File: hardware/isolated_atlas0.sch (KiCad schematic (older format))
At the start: 15 parts, among them J201 CONN_01X02, P2 ATLAS_EC_PROBE, U201 ADM3260, U202 ATLAS_EC

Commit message: Upgrade to Kicad 5.
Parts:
- C201, C202, C203, C204, C205, C206: symbol C -> fk-atlas-rescue:C
- J201: symbol CONN_01X02 -> fk-atlas-rescue:CONN_01X02
- P2: symbol WATER_PROBE -> fk-atlas-rescue:WATER_PROBE
- R201, R202, R203, R204, R205: symbol R -> fk-atlas-rescue:R
- U201: symbol adm3260 -> fk-atlas-rescue:adm3260
- U202: symbol ATLAS_SENSOR -> conservify:ATLAS_SENSOR
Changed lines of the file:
@@
-EESchema Schematic File Version 2
-LIBS:conservify
+EESchema Schematic File Version 4
 LIBS:fk-atlas-cache
-EELAYER 25 0
+EELAYER 26 0
 EELAYER END
 $Descr A4 11693 8268
@@
 $EndDescr
 $Comp
-L adm3260 U201
+L fk-atlas-rescue:adm3260 U201
 U 1 1 5948D478
 P 4400 2900
@@
 $EndComp
 $Comp
-L C C203
+L fk-atlas-rescue:C C203
 U 1 1 594C2CF3
 P 5650 3800
@@
 $EndComp
 $Comp
-L C C204
+L fk-atlas-rescue:C C204
 U 1 1 5948D57F
 P 5650 4100
@@
 $EndComp
 $Comp
-L C C205
+L fk-atlas-rescue:C C205
 U 1 1 594C2CFE
 P 5650 4400
@@
 $EndComp
 $Comp
-L C C206
+L fk-atlas-rescue:C C206
 U 1 1 594C2D01
 P 5650 4650
@@
 $EndComp
 $Comp
-L C C201
+L fk-atlas-rescue:C C201
 U 1 1 594C2D06
 P 2900 3800
@@
 $EndComp
 $Comp
-L C C202
+L fk-atlas-rescue:C C202
 U 1 1 594C2D08
 P 2900 4100
@@
 $EndComp
 $Comp
-L R R201
+L fk-atlas-rescue:R R201
 U 1 1 594C2D0E
 P 5650 3300
@@
 $EndComp
 $Comp
-L R R202
+L fk-atlas-rescue:R R202
 U 1 1 594C2D12
 P 6250 2700
@@
 $EndComp
 $Comp
-L R R204
+L fk-atlas-rescue:R R204
 U 1 1 5948E389
 P 6700 2700
@@
 $EndComp
 $Comp
-L R R203
+L fk-atlas-rescue:R R203
 U 1 1 594C2D17
 P 6300 3250
@@
 $EndComp
 $Comp
-L R R205
+L fk-atlas-rescue:R R205
 U 1 1 594C2D1E
 P 6800 3250
@@
 $EndComp
 $Comp
-L VCC #PWR057
+L fk-atlas-rescue:VCC #PWR057
 U 1 1 594C2D26
 P 2450 3750
@@
 $EndComp
 $Comp
-L VCC #PWR058
+L fk-atlas-rescue:VCC #PWR058
 U 1 1 594C2D28
 P 2450 2350
@@
 $EndComp
 $Comp
-L ATLAS_SENSOR U202
+L conservify:ATLAS_SENSOR U202
 U 1 1 594C2D33
 P 8550 2900
@@
 $EndComp
 $Comp
-L CONN_01X02 J201
+L fk-atlas-rescue:CONN_01X02 J201
 U 1 1 59A1BC7B
 P 10050 2950
@@
 $EndComp
 $Comp
-L WATER_PROBE P2
+L fk-atlas-rescue:WATER_PROBE P2
 U 1 1 59D297CD
 P 8800 3550

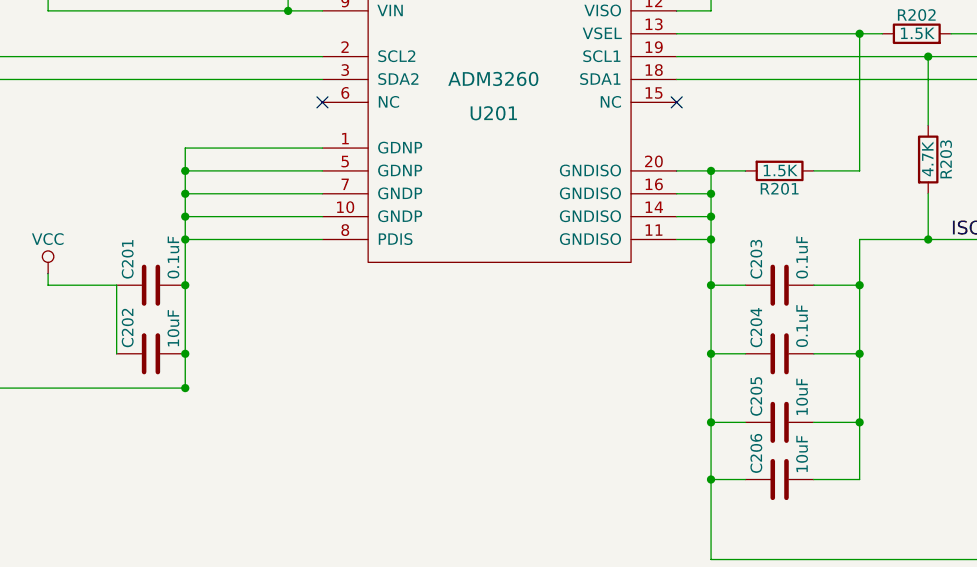
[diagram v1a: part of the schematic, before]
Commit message: Consistent part values across our schematics.
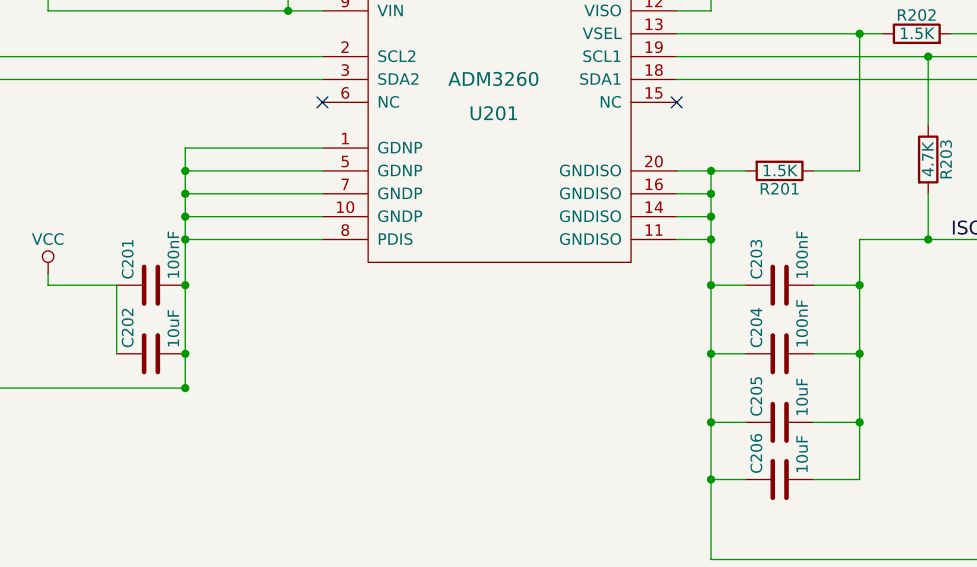
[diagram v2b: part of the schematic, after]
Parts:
- C201, C203, C204: value 0.1uF -> 100nF

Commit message: Part updates.
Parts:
- C201, C203, C204: Critical (none) -> (none); MFN (none) -> Murata Electronics; MFP (none) -> GRM188R71H104KA93D; Notes (none) -> (none); Package (none) -> (none); Source (none) -> ANY; Subsystem (none) -> (none); Supplier1 (none) -> mouser
- C202, C205, C206: Critical (none) -> (none); MFN (none) -> Taiyo Yuden; MFP (none) -> LMK107BBJ106KALT; Notes (none) -> (none); Package (none) -> (none); Source (none) -> ANY; Subsystem (none) -> (none); Supplier1 (none) -> mouser; spn1 81-GRM188R60J106ME47 -> 963-LMK107BBJ106KALT
- J201: Critical (none) -> (none); MFN (none) -> Amphenol RF; MFP (none) -> 031-5431; Notes (none) -> (none); Package (none) -> (none); Source (none) -> ANY; Subsystem (none) -> (none); Supplier1 (none) -> mouser
- P2: Critical (none) -> (none); MFN (none) -> (none); MFP (none) -> (none); Notes (none) -> (none); Package (none) -> (none); SPN1 (none) -> (none); Source (none) -> ANY; Subsystem (none) -> (none); Supplier1 (none) -> (none)
- R201, R202, R204: Critical (none) -> (none); MFN (none) -> (none); MFP (none) -> (none); Notes (none) -> (none); Package (none) -> (none); Source (none) -> ANY; Subsystem (none) -> (none); Supplier1 (none) -> (none)
- R203, R205: Critical (none) -> (none); MFN (none) -> Yageo; MFP (none) -> AF0603JR-074K7L; Notes (none) -> (none); Package (none) -> (none); Source (none) -> ANY; Subsystem (none) -> (none); Supplier1 (none) -> mouser
- U201: Critical (none) -> (none); MFN (none) -> Analog Devices / Linear Technology; MFP (none) -> ADM3260ARSZ; Notes (none) -> (none); Package (none) -> (none); Source (none) -> ANY; Subsystem (none) -> (none); Supplier1 (none) -> mouser
- U202: Critical (none) -> (none); MFN (none) -> (none); MFP (none) -> (none); Notes (none) -> (none); Package (none) -> (none); SPN1 (none) -> (none); Source (none) -> ANY; Subsystem (none) -> (none); Supplier1 (none) -> atlas

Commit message: Fix DRC in schematic mode.
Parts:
- C201, C202, C203, C204, C205, C206: symbol fk-atlas-rescue:C -> conservify:CAPACITOR_CERAMIC
- J201: symbol fk-atlas-rescue:CONN_01X02 -> conservify:CONN_01x02
- P2: symbol fk-atlas-rescue:WATER_PROBE -> conservify:ATLAS_WATER_PROBE
- R201, R202, R203, R204, R205: symbol fk-atlas-rescue:R -> conservify:R
- U201: symbol fk-atlas-rescue:adm3260 -> conservify:ADM3260
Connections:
- wire segments 52 -> 78
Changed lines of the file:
@@
 $EndDescr
 $Comp
-L fk-atlas-rescue:adm3260 U201
+L conservify:ADM3260 U201
 U 1 1 5948D478
 P 4400 2900
@@
 $EndComp
 $Comp
-L fk-atlas-rescue:C C203
+L conservify:CAPACITOR_CERAMIC C203
 U 1 1 594C2CF3
 P 5650 3800
@@
 $EndComp
 $Comp
-L fk-atlas-rescue:C C204
+L conservify:CAPACITOR_CERAMIC C204
 U 1 1 5948D57F
 P 5650 4100
@@
 $EndComp
 $Comp
-L fk-atlas-rescue:C C205
+L conservify:CAPACITOR_CERAMIC C205
 U 1 1 594C2CFE
 P 5650 4400
@@
 $EndComp
 $Comp
-L fk-atlas-rescue:C C206
+L conservify:CAPACITOR_CERAMIC C206
 U 1 1 594C2D01
 P 5650 4650
@@
 $EndComp
 $Comp
-L fk-atlas-rescue:C C201
+L conservify:CAPACITOR_CERAMIC C201
 U 1 1 594C2D06
 P 2900 3800
@@
 $EndComp
 $Comp
-L fk-atlas-rescue:C C202
+L conservify:CAPACITOR_CERAMIC C202
 U 1 1 594C2D08
 P 2900 4100
@@
 $EndComp
 $Comp
-L fk-atlas-rescue:R R201
+L conservify:R R201
 U 1 1 594C2D0E
 P 5650 3300
@@
 $EndComp
 $Comp
-L fk-atlas-rescue:R R202
+L conservify:R R202
 U 1 1 594C2D12
 P 6250 2700
@@
 $EndComp
 $Comp
-L fk-atlas-rescue:R R204
+L conservify:R R204
 U 1 1 5948E389
 P 6700 2700
@@
 $EndComp
 $Comp
-L fk-atlas-rescue:R R203
+L conservify:R R203
 U 1 1 594C2D17
 P 6300 3250
@@
 $EndComp
 $Comp
-L fk-atlas-rescue:R R205
+L conservify:R R205
 U 1 1 594C2D1E
 P 6800 3250
@@
 $EndComp
 $Comp
-L fk-atlas-rescue:VCC #PWR057
+L conservify:VCC #PWR057
 U 1 1 594C2D26
 P 2450 3750
@@
 $EndComp
 $Comp
-L fk-atlas-rescue:VCC #PWR058
+L conservify:VCC #PWR058
 U 1 1 594C2D28
 P 2450 2350
@@
 $EndComp
 $Comp
-L fk-atlas-rescue:CONN_01X02 J201
+L conservify:CONN_01x02 J201
 U 1 1 59A1BC7B
-P 10050 2950
-F 0 "J201" H 10050 3100 50  0000 C CNN
-F 1 "CONN_01X02" V 10150 2950 50  0000 C CNN
-F 2 "conservify:BNC" H 10050 2950 50  0001 C CNN
-F 3 "" H 10050 2950 50  0001 C CNN
-F 4 " " H 10050 3200 50  0001 C CNN "Critical"
-F 5 "Amphenol RF" H 10050 3200 50  0001 C CNN "MFN"
-F 6 "031-5431" H 10050 3200 50  0001 C CNN "MFP"
-F 7 " " H 10050 3200 50  0001 C CNN "Notes"
-F 8 " " H 10050 3200 50  0001 C CNN "Package"
-F 9 "ANY" H 10050 3200 50  0001 C CNN "Source"
-F 10 " " H 10050 3200 50  0001 C CNN "Subsystem"
-F 11 "mouser" H 10050 3200 50  0001 C CNN "Supplier1"
-F 12 "0" H 10050 3200 50  0001 C CNN "price"
-F 13 "523-31-5431" H 200 0   50  0001 C CNN "spn1"
-	1    10050 2950
-	1    0    0    -1
-$EndComp
-$Comp
-L fk-atlas-rescue:WATER_PROBE P2
+P 10050 2900
+F 0 "J201" H 10050 3050 50  0000 C CNN
+F 1 "CONN_01X02" V 10150 2900 50  0000 C CNN
+F 2 "conservify:BNC" H 10050 2900 50  0001 C CNN
+F 3 "" H 10050 2900 50  0001 C CNN
+F 4 " " H 10050 3150 50  0001 C CNN "Critical"
+F 5 "Amphenol RF" H 10050 3150 50  0001 C CNN "MFN"
+F 6 "031-5431" H 10050 3150 50  0001 C CNN "MFP"
+F 7 " " H 10050 3150 50  0001 C CNN "Notes"
+F 8 " " H 10050 3150 50  0001 C CNN "Package"
+F 9 "ANY" H 10050 3150 50  0001 C CNN "Source"
+F 10 " " H 10050 3150 50  0001 C CNN "Subsystem"
+F 11 "mouser" H 10050 3150 50  0001 C CNN "Supplier1"
+F 12 "0" H 10050 3150 50  0001 C CNN "price"
+F 13 "523-31-5431" H 200 -50 50  0001 C CNN "spn1"
+	1    10050 2900
+	1    0    0    -1
+$EndComp
+$Comp
+L conservify:ATLAS_WATER_PROBE P2
 U 1 1 59D297CD
 P 8800 3550
@@
 F 12 " " H 8800 3650 50  0001 C CNN "Supplier1"
 	1    8800 3550
+	1    0    0    -1
+$EndComp
+$Comp
+L conservify:PWR_FLAG #FLG0106
+U 1 1 5BCC03FC
+P 7400 4900
+F 0 "#FLG0106" H 7400 4975 50  0001 C CNN
+F 1 "PWR_FLAG" H 7400 5050 50  0000 C CNN
+F 2 "" H 7400 4900 50  0001 C CNN
+F 3 "~" H 7400 4900 50  0001 C CNN
+	1    7400 4900
 	1    0    0    -1
 $EndComp
@@
 EC_PGND
 Wire Wire Line
-	5200 3300 5500 3300
-Wire Wire Line
-	5350 3300 5350 5000
+	5200 3300 5350 3300
+Wire Wire Line
+	5350 3300 5350 3400
 Wire Wire Line
 	5350 3600 5200 3600
@@
 	5800 3800 6000 3800
 Wire Wire Line
-	6000 3600 6000 4650
+	6000 3600 6000 3800
 Wire Wire Line
 	6000 4650 5800 4650
@@
 	5800 4100 6000 4100
 Wire Wire Line
-	5200 2800 7800 2800
-Wire Wire Line
-	5200 2900 7800 2900
-Wire Wire Line
-	5200 2700 6100 2700
+	5200 2800 6300 2800
+Wire Wire Line
+	5200 2900 6800 2900
+Wire Wire Line
+	5200 2700 6000 2700
 Wire Wire Line
 	6000 2700 6000 3300
@@
 	5350 2600 5350 2500
 Wire Wire Line
-	5200 2500 7400 2500
+	5200 2500 5350 2500
 Wire Wire Line
 	6900 2500 6900 2700
@@
 	6300 3400 6300 3600
 Wire Wire Line
-	6000 3600 6800 3600
+	6000 3600 6300 3600
 Wire Wire Line
 	6800 3600 6800 3400
 Wire Wire Line
-	2450 2600 3650 2600
-Wire Wire Line
-	2450 2350 2450 2600
+	2450 2600 3500 2600
+Wire Wire Line
+	2450 2350 2450 2450
 Wire Wire Line
 	3650 2500 3500 2500
@@
 	3650 3200 3050 3200
 Wire Wire Line
-	3050 3200 3050 4250
+	3050 3200 3050 3300
 Wire Wire Line
 	3050 4250 1750 4250
@@
 Wire Wire Line
 	9450 3000 9850 3000
+Wire Wire Line
+	5350 3500 5350 3600
+Wire Wire Line
+	5350 3400 5350 3500
+Wire Wire Line
+	5350 3600 5350 3800
+Wire Wire Line
+	5350 4400 5350 4650
+Wire Wire Line
+	5350 4100 5350 4400
+Wire Wire Line
+	5350 3800 5350 4100
+Wire Wire Line
+	6000 4400 6000 4650
+Wire Wire Line
+	6000 4100 6000 4400
+Wire Wire Line
+	5350 3300 5500 3300
+Wire Wire Line
+	5350 2500 6900 2500
+Wire Wire Line
+	6000 2700 6100 2700
+Wire Wire Line
+	6300 2800 7800 2800
+Wire Wire Line
+	6800 2900 7800 2900
+Wire Wire Line
+	3500 2600 3650 2600
+Wire Wire Line
+	3050 3800 3050 4100
+Wire Wire Line
+	3050 4100 3050 4250
+Wire Wire Line
+	3050 3600 3050 3800
+Wire Wire Line
+	3050 3500 3050 3600
+Wire Wire Line
+	3050 3400 3050 3500
+Wire Wire Line
+	3050 3300 3050 3400
+Wire Wire Line
+	2450 2450 2450 2600
+Wire Wire Line
+	5350 4650 5350 5000
+Wire Wire Line
+	6300 3600 6800 3600
+Wire Wire Line
+	6000 3800 6000 4100
+Wire Wire Line
+	6900 2500 7400 2500
+Wire Wire Line
+	7400 4900 7400 5000
 Connection ~ 5350 3500
 Connection ~ 5350 3400
@@
 Connection ~ 6300 3600
 Connection ~ 6000 3800
-Connection ~ 3050 4250
 Connection ~ 6900 2500
 NoConn ~ 3650 3000

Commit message: Drop prototype Atlas modules - focus on getting OEM boards working.
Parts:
- U202: footprint conservify:ATLAS_SENSOR_BOARD_COMBO -> conservify:ATLAS_SENSOR_BOARD_OEM
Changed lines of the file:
@@
 F 0 "U202" H 8150 2550 60  0000 C CNN
 F 1 "ATLAS_EC" H 8600 2850 60  0000 C CNN
-F 2 "conservify:ATLAS_SENSOR_BOARD_COMBO" H 8550 2900 60  0001 C CNN
+F 2 "conservify:ATLAS_SENSOR_BOARD_OEM" H 8550 2900 60  0001 C CNN
 F 3 "" H 8550 2900 60  0001 C CNN
 F 4 " " H 8150 2650 50  0001 C CNN "Critical"

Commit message: Trying out some test points.
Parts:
- added J10, J9: CONN_01x02, conservify:TP_Pads_D1.5mm_1x2, symbol conservify:CONN_01x02
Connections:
- wire segments 78 -> 82
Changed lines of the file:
@@
 NoConn ~ 3650 3000
 NoConn ~ 5200 3000
+Text Label 8350 4450 0    60   ~ 0
+ISO_GND
+Text Label 8350 4350 0    60   ~ 0
+ISO_VCC
+Text Label 8350 4100 0    60   ~ 0
+ISO_SCL
+Text Label 8350 4200 0    60   ~ 0
+ISO_SDA
+Wire Wire Line
+	8350 4100 8750 4100
+Wire Wire Line
+	8750 4200 8350 4200
+Wire Wire Line
+	8350 4350 8750 4350
+Wire Wire Line
+	8750 4450 8350 4450
+$Comp
+L conservify:CONN_01x02 J9
+U 1 1 5C0B31F6
+P 8950 4100
+F 0 "J9" H 9029 4092 50  0000 L CNN
+F 1 "CONN_01x02" H 9029 4001 50  0000 L CNN
+F 2 "conservify:TP_Pads_D1.5mm_1x2" H 8950 4100 50  0001 C CNN
+F 3 "" H 8950 4100 50  0001 C CNN
+	1    8950 4100
+	1    0    0    -1
+$EndComp
+$Comp
+L conservify:CONN_01x02 J10
+U 1 1 5C0B3270
+P 8950 4350
+F 0 "J10" H 9029 4342 50  0000 L CNN
+F 1 "CONN_01x02" H 9029 4251 50  0000 L CNN
+F 2 "conservify:TP_Pads_D1.5mm_1x2" H 8950 4350 50  0001 C CNN
+F 3 "" H 8950 4350 50  0001 C CNN
+	1    8950 4350
+	1    0    0    -1
+$EndComp
 $EndSCHEMATC

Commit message: Add orientation indicator to SWD fp.
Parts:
- J10, J9: Critical (none) -> (none); MFN (none) -> (none); MFP (none) -> (none); Notes (none) -> (none); Package (none) -> (none); SPN1 (none) -> (none); Source (none) -> ANY; Subsystem (none) -> (none); Supplier1 (none) -> (none)
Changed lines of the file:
@@
+	1    0    0    -1
+$EndComp
+$Comp
+L conservify:CONN_01x02 J9
+U 1 1 5C0B31F6
+P 8950 4100
+F 0 "J9" H 9029 4092 50  0000 L CNN
+F 1 "CONN_01x02" H 9029 4001 50  0000 L CNN
+F 2 "conservify:TP_Pads_D1.5mm_1x2" H 8950 4100 50  0001 C CNN
+F 3 "" H 8950 4100 50  0001 C CNN
+F 4 " " H 9029 4192 50  0001 C CNN "Critical"
+F 5 " " H 9029 4192 50  0001 C CNN "MFN"
+F 6 " " H 9029 4192 50  0001 C CNN "MFP"
+F 7 " " H 9029 4192 50  0001 C CNN "Notes"
+F 8 " " H 9029 4192 50  0001 C CNN "Package"
+F 9 " " H 9029 4192 50  0001 C CNN "SPN1"
+F 10 "ANY" H 9029 4192 50  0001 C CNN "Source"
+F 11 " " H 9029 4192 50  0001 C CNN "Subsystem"
+F 12 " " H 9029 4192 50  0001 C CNN "Supplier1"
+	1    8950 4100
+	1    0    0    -1
+$EndComp
+$Comp
+L conservify:CONN_01x02 J10
+U 1 1 5C0B3270
+P 8950 4350
+F 0 "J10" H 9029 4342 50  0000 L CNN
+F 1 "CONN_01x02" H 9029 4251 50  0000 L CNN
+F 2 "conservify:TP_Pads_D1.5mm_1x2" H 8950 4350 50  0001 C CNN
+F 3 "" H 8950 4350 50  0001 C CNN
+F 4 " " H 9029 4442 50  0001 C CNN "Critical"
+F 5 " " H 9029 4442 50  0001 C CNN "MFN"
+F 6 " " H 9029 4442 50  0001 C CNN "MFP"
+F 7 " " H 9029 4442 50  0001 C CNN "Notes"
+F 8 " " H 9029 4442 50  0001 C CNN "Package"
+F 9 " " H 9029 4442 50  0001 C CNN "SPN1"
+F 10 "ANY" H 9029 4442 50  0001 C CNN "Source"
+F 11 " " H 9029 4442 50  0001 C CNN "Subsystem"
+F 12 " " H 9029 4442 50  0001 C CNN "Supplier1"
+	1    8950 4350
 	1    0    0    -1
 $EndComp
@@
 Text Label 9450 2900 0    60   ~ 0
 EC_PGND
+Text Label 8350 4450 0    60   ~ 0
+ISO_GND
+Text Label 8350 4350 0    60   ~ 0
+ISO_VCC
+Text Label 8350 4100 0    60   ~ 0
+ISO_SCL
+Text Label 8350 4200 0    60   ~ 0
+ISO_SDA
 Wire Wire Line
 	5200 3300 5350 3300
@@
 Wire Wire Line
 	7400 4900 7400 5000
+Wire Wire Line
+	8350 4100 8750 4100
+Wire Wire Line
+	8750 4200 8350 4200
+Wire Wire Line
+	8350 4350 8750 4350
+Wire Wire Line
+	8750 4450 8350 4450
 Connection ~ 5350 3500
 Connection ~ 5350 3400
@@
 NoConn ~ 3650 3000
 NoConn ~ 5200 3000
-Text Label 8350 4450 0    60   ~ 0
-ISO_GND
-Text Label 8350 4350 0    60   ~ 0
-ISO_VCC
-Text Label 8350 4100 0    60   ~ 0
-ISO_SCL
-Text Label 8350 4200 0    60   ~ 0
-ISO_SDA
-Wire Wire Line
-	8350 4100 8750 4100
-Wire Wire Line
-	8750 4200 8350 4200
-Wire Wire Line
-	8350 4350 8750 4350
-Wire Wire Line
-	8750 4450 8350 4450
-$Comp
-L conservify:CONN_01x02 J9
-U 1 1 5C0B31F6
-P 8950 4100
-F 0 "J9" H 9029 4092 50  0000 L CNN
-F 1 "CONN_01x02" H 9029 4001 50  0000 L CNN
-F 2 "conservify:TP_Pads_D1.5mm_1x2" H 8950 4100 50  0001 C CNN
-F 3 "" H 8950 4100 50  0001 C CNN
-	1    8950 4100
-	1    0    0    -1
-$EndComp
-$Comp
-L conservify:CONN_01x02 J10
-U 1 1 5C0B3270
-P 8950 4350
-F 0 "J10" H 9029 4342 50  0000 L CNN
-F 1 "CONN_01x02" H 9029 4251 50  0000 L CNN
-F 2 "conservify:TP_Pads_D1.5mm_1x2" H 8950 4350 50  0001 C CNN
-F 3 "" H 8950 4350 50  0001 C CNN
-	1    8950 4350
-	1    0    0    -1
-$EndComp
 $EndSCHEMATC
